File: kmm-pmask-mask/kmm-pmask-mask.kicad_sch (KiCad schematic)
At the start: 68 parts, among them J1 F31L-1A7H1-11030, U1 MS5611-01BA, U10 MAX30101EFD_T, U11 SHT40-AD1B-R3, U12 SHT40-AD1B-R3, U13 TMP117MAIDRVR, U14 TMP117MAIDRVR, U15 TCA9546APW, U2 MAX30101EFD_T, U3 SHT40-AD1B-R3, U4 TMP117MAIDRVR, U5 MS5611-01BA, U6 MS5611-01BA, U7 MS5611-01BA, U8 MAX30101EFD_T, U9 MAX30101EFD_T

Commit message: track cleanup
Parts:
- TP1, TP10, TP11, TP12, TP13, TP14, TP15, TP16, TP17, TP2, TP3, TP4, TP5, TP6, TP7, TP8, TP9: footprint TestPoint:TestPoint_Pad_D1.5mm -> TestPoint:TestPoint_Pad_D1.0mm
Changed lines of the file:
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@@
 			)
 		)
-		(property "Footprint" "TestPoint:TestPoint_Pad_D1.5mm"
+		(property "Footprint" "TestPoint:TestPoint_Pad_D1.0mm"
 			(at 199.39 40.64 0)
 			(hide yes)
@@
 			)
 		)
-		(property "Footprint" "TestPoint:TestPoint_Pad_D1.5mm"
+		(property "Footprint" "TestPoint:TestPoint_Pad_D1.0mm"
 			(at 186.69 40.64 0)
 			(hide yes)
@@
 			)
 		)
-		(property "Footprint" "TestPoint:TestPoint_Pad_D1.5mm"
+		(property "Footprint" "TestPoint:TestPoint_Pad_D1.0mm"
 			(at 262.89 93.98 0)
 			(hide yes)
@@
 			)
 		)
-		(property "Footprint" "TestPoint:TestPoint_Pad_D1.5mm"
+		(property "Footprint" "TestPoint:TestPoint_Pad_D1.0mm"
 			(at 163.83 27.94 0)
 			(hide yes)
@@
 			)
 		)
-		(property "Footprint" "TestPoint:TestPoint_Pad_D1.5mm"
+		(property "Footprint" "TestPoint:TestPoint_Pad_D1.0mm"
 			(at 173.99 40.64 0)
 			(hide yes)
@@
 			)
 		)
-		(property "Footprint" "TestPoint:TestPoint_Pad_D1.5mm"
+		(property "Footprint" "TestPoint:TestPoint_Pad_D1.0mm"
 			(at 298.45 100.33 0)
 			(hide yes)
@@
 			)
 		)
-		(property "Footprint" "TestPoint:TestPoint_Pad_D1.5mm"
+		(property "Footprint" "TestPoint:TestPoint_Pad_D1.0mm"
 			(at 189.23 27.94 0)
 			(hide yes)
@@
 			)
 		)
-		(property "Footprint" "TestPoint:TestPoint_Pad_D1.5mm"
+		(property "Footprint" "TestPoint:TestPoint_Pad_D1.0mm"
 			(at 176.53 27.94 0)
 			(hide yes)
@@
 			)
 		)
-		(property "Footprint" "TestPoint:TestPoint_Pad_D1.5mm"
+		(property "Footprint" "TestPoint:TestPoint_Pad_D1.0mm"
 			(at 341.63 96.52 0)
 			(hide yes)
@@
 			)
 		)
-		(property "Footprint" "TestPoint:TestPoint_Pad_D1.5mm"
+		(property "Footprint" "TestPoint:TestPoint_Pad_D1.0mm"
 			(at 252.73 100.33 0)
 			(hide yes)
@@
 			)
 		)
-		(property "Footprint" "TestPoint:TestPoint_Pad_D1.5mm"
+		(property "Footprint" "TestPoint:TestPoint_Pad_D1.0mm"
 			(at 313.69 100.33 0)
 			(hide yes)
@@
 			)
 		)
-		(property "Footprint" "TestPoint:TestPoint_Pad_D1.5mm"
+		(property "Footprint" "TestPoint:TestPoint_Pad_D1.0mm"
 			(at 323.85 93.98 0)
 			(hide yes)
@@
 			)
 		)
-		(property "Footprint" "TestPoint:TestPoint_Pad_D1.5mm"
+		(property "Footprint" "TestPoint:TestPoint_Pad_D1.0mm"
 			(at 283.21 100.33 0)
 			(hide yes)
@@
 			)
 		)
-		(property "Footprint" "TestPoint:TestPoint_Pad_D1.5mm"
+		(property "Footprint" "TestPoint:TestPoint_Pad_D1.0mm"
 			(at 267.97 100.33 0)
 			(hide yes)
@@
 			)
 		)
-		(property "Footprint" "TestPoint:TestPoint_Pad_D1.5mm"
+		(property "Footprint" "TestPoint:TestPoint_Pad_D1.0mm"
 			(at 308.61 93.98 0)
 			(hide yes)
@@
 			)
 		)
-		(property "Footprint" "TestPoint:TestPoint_Pad_D1.5mm"
+		(property "Footprint" "TestPoint:TestPoint_Pad_D1.0mm"
 			(at 278.13 93.98 0)
 			(hide yes)
@@
 			)
 		)
-		(property "Footprint" "TestPoint:TestPoint_Pad_D1.5mm"
+		(property "Footprint" "TestPoint:TestPoint_Pad_D1.0mm"
 			(at 293.37 93.98 0)
 			(hide yes)

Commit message: Add fiducials, missing 3D
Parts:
- added FID1, FID2, FID3: Fiducial, Fiducial:Fiducial_1mm_Mask3mm, symbol Mechanical:Fiducial
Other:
- note added: "Mechanical"

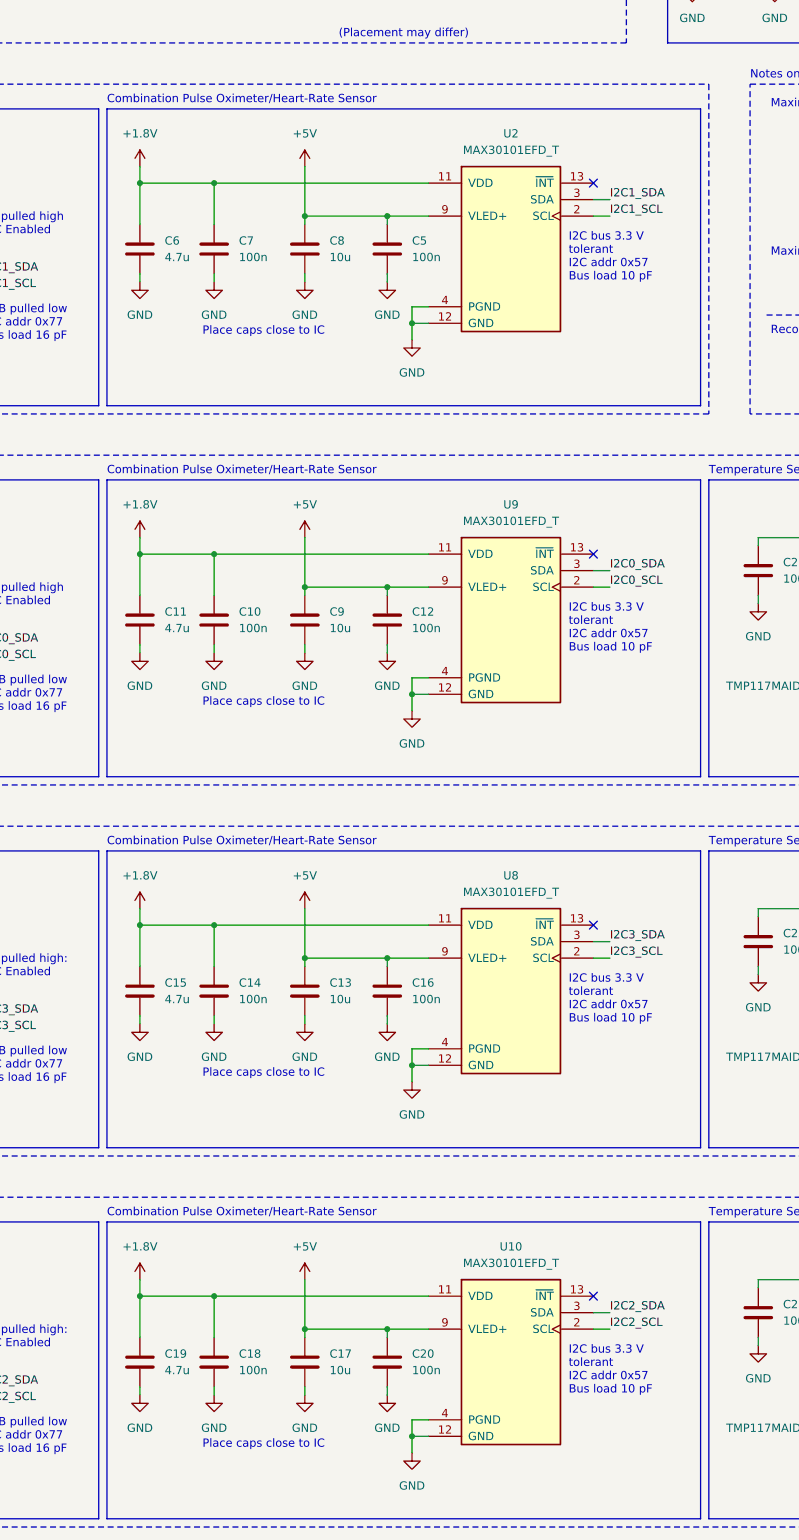
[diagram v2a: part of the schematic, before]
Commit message: Add pull-ups for unused interrupt line, just in case
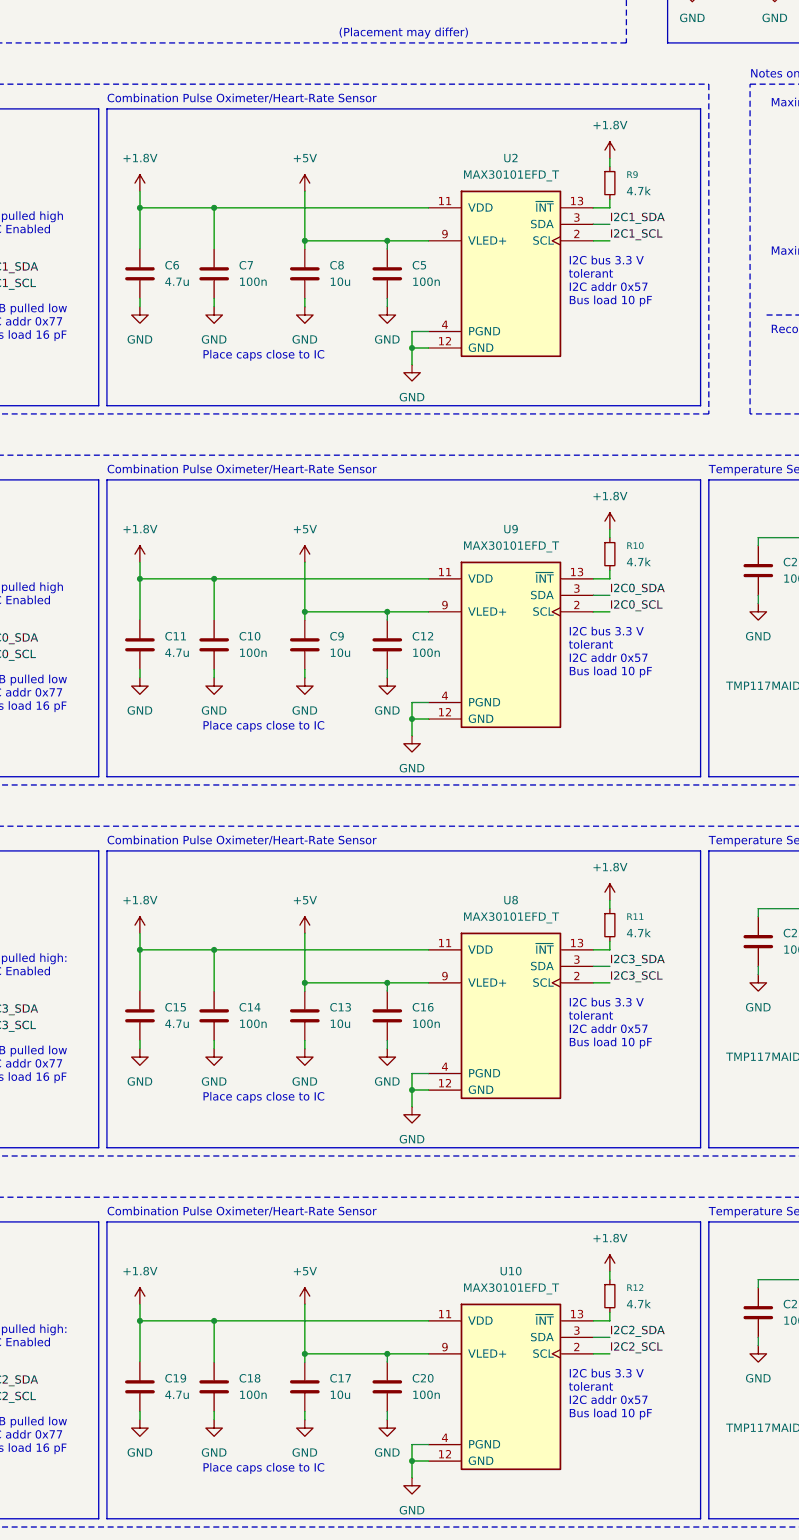
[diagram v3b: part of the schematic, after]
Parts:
- added R10, R11, R12, R9: 4.7k, Resistor_SMD:R_0201_0603Metric_Pad0.64x0.40mm_HandSolder, symbol Device:R_Small
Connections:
- net +1.8V: now also R10.1, R11.1, R12.1, R9.1
- net at U10.13 (~{INT}): now also R12.2
- net at U2.13 (~{INT}): now also R9.2
- net at U9.13 (~{INT}): now also R10.2
- net at U8.13 (~{INT}): now also R11.2
- no-connect marks 11 -> 7
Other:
- moved on the sheet: C10, C11, C12, C13, C14, C15, C16, C17, C18, C19, C20, C5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
